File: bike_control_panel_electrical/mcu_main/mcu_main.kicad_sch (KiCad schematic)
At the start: 11 parts, among them U1 ESP32-S3-WROOM-1, U2 USB_C_connector

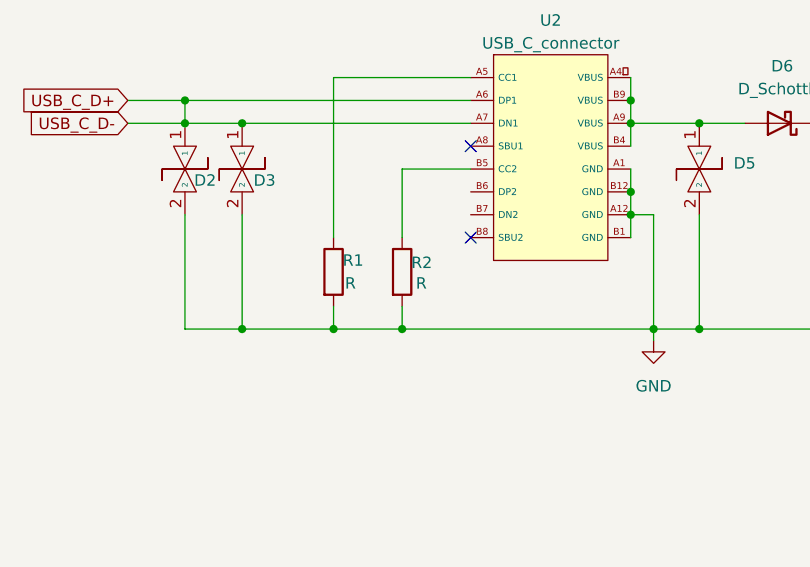
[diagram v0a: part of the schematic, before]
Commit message: res value 4.7 for UCB_C cc pins
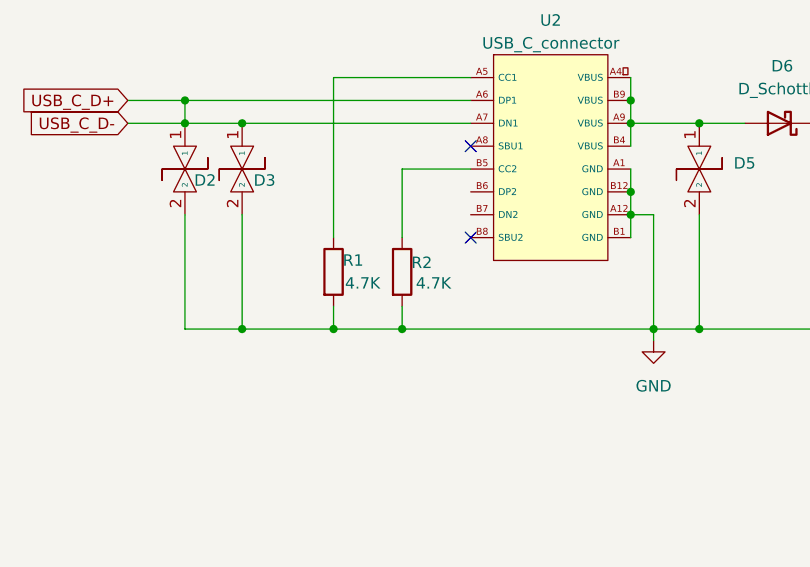
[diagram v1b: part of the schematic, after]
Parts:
- R1, R2: value R -> 4.7K
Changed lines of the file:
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@@
 			)
 		)
-		(property "Value" "R"
+		(property "Value" "4.7K"
 			(at 165.354 53.34 0)
 			(effects
@@
 			)
 		)
-		(property "Value" "R"
+		(property "Value" "4.7K"
 			(at 157.48 53.34 0)
 			(effects
